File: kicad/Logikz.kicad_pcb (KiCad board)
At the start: 2 copper layers, 93.2 x 85 mm, 24 parts, among them Q1 NPN, Q2 NPN, Q3 NPN, Q4 NPN, Q5 NPN, Q6 NPN, SW1 SW_Push, SW2 SW_Push, SW3 SW_Push, SW4 SW_Push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

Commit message: silkscreens to the pcb
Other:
- board text added: "Date: 12 June 2025 By: Ankush Roy Name: Logikz Event: Solder"

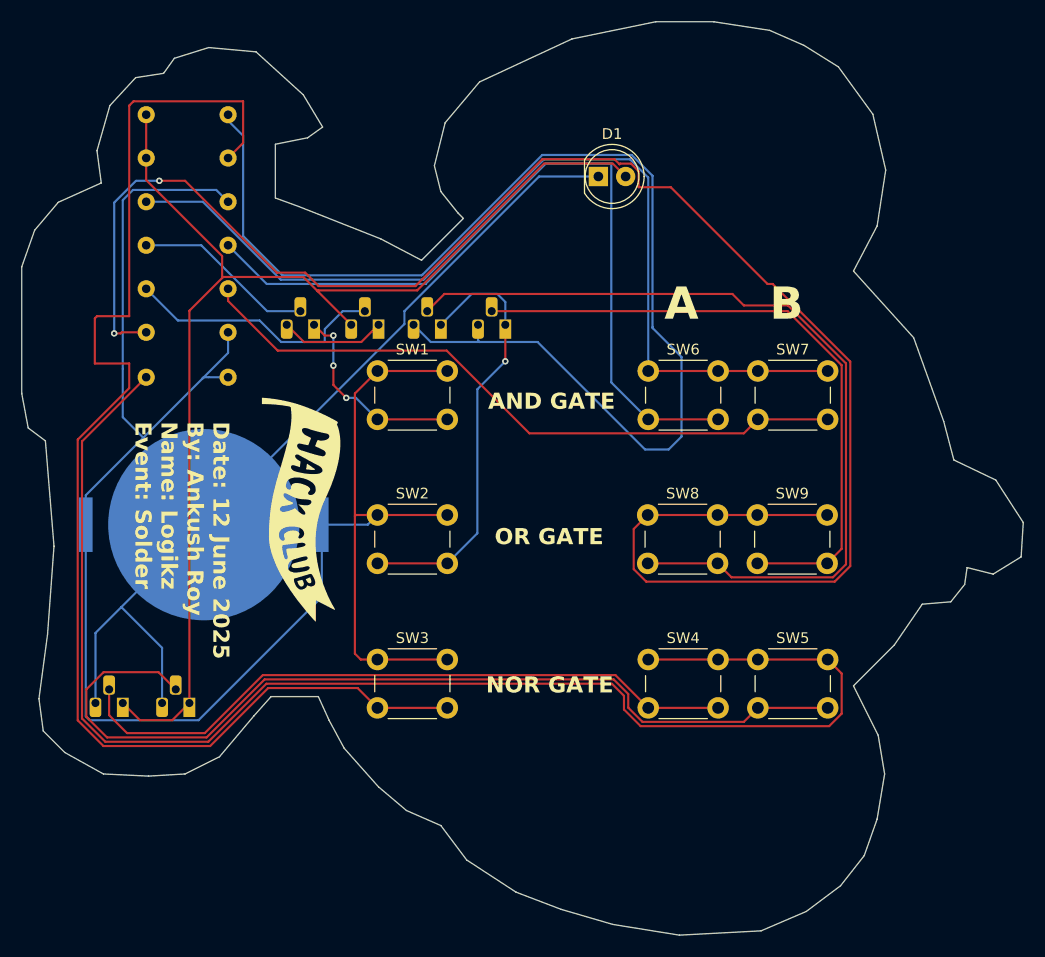
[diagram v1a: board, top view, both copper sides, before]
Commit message: Changed the wires to roundedgit add!! Looks very cool!
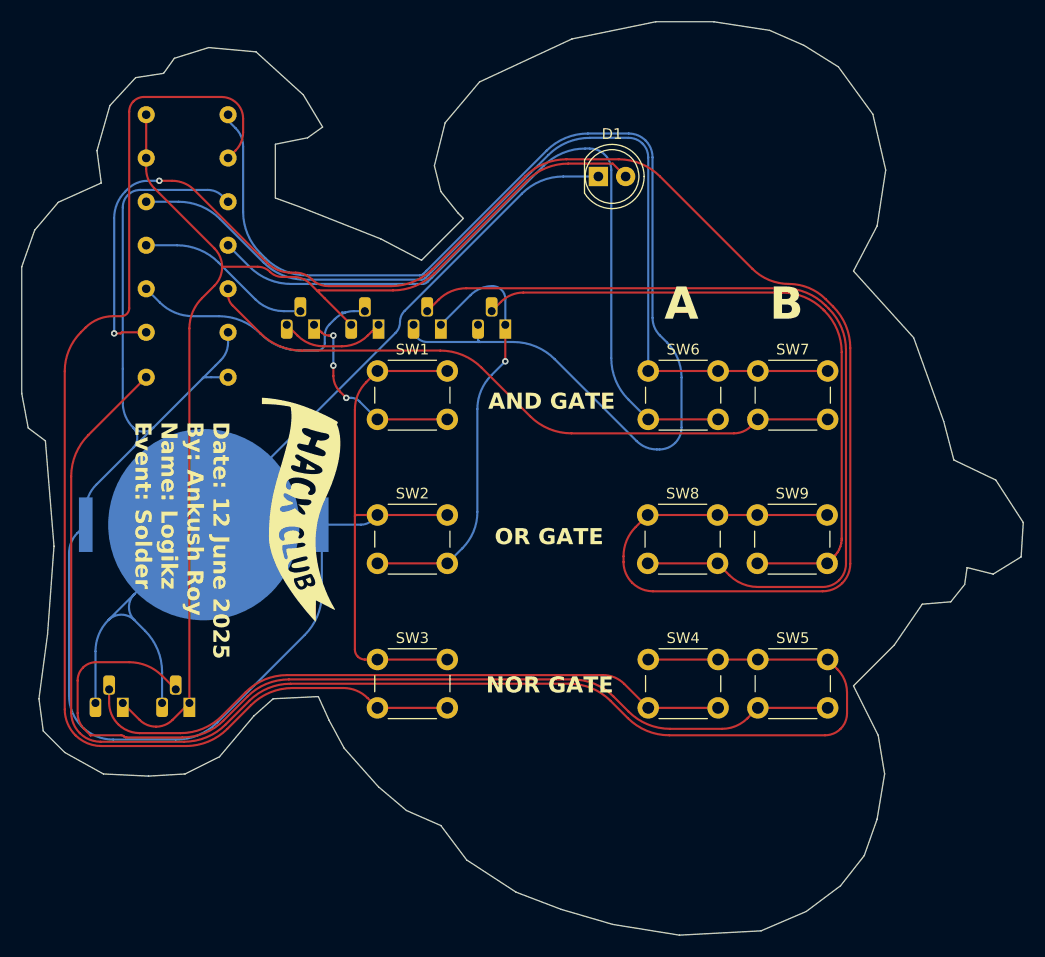
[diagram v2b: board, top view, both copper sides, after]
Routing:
- net Net-(BT1-+): track 167.5 -> 172.9 mm
- net Net-(R4-Pad1): track 120.5 -> 115.5 mm
- net Net-(Q4-B): track 60.2 -> 62.8 mm
- net Net-(BT1--): track 82.1 -> 84.8 mm
- net Net-(Q3-B): track 80.5 -> 83.1 mm
- net Net-(R5-Pad2): track 89.8 -> 92.0 mm
- net Net-(Q3-E): track 114.2 -> 116.0 mm
- net Net-(Q6-B): track 87.1 -> 88.8 mm
- net Net-(R8-Pad2): track 164.8 -> 165.7 mm
- net Net-(R2-Pad2): track 133.2 -> 134.2 mm
- net Net-(R7-Pad1): track 62.6 -> 61.6 mm
- net Net-(Q5-B): track 63.3 -> 62.3 mm
- net Net-(D1-A): track 114.4 -> 113.7 mm
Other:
- outline, holes or cut-outs redrawn
